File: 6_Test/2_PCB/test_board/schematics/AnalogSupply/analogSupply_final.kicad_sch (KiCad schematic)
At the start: 17 parts

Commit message: Corrections to schematic 11_20_24
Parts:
- C? (x4): value CL05B104KP5NNNC -> 100n
- C? (x3): value CL10A475KP8NNNC -> 4.7u
- R?: value RC0402JR-071KL -> 1k
- R?: value RC0402JR-071KL -> 4.7k
- R? (x3): value PV37W103C01B00 -> 10k
- U? (x2): footprint KS-6_ADI -> opampADA4807Footprints:KS-6_ADI
- U?: value TPS74501PDRVR -> LDO_Analog_Supply
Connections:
- net AVSS: no longer C?.1, C?.2
- net GND: now also C?.1, C?.2
- net at R?.2, U?.2 (FB): no longer R?.2
- net at R?.3: now also R?.2
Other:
- moved on the sheet: C?, L?, R?

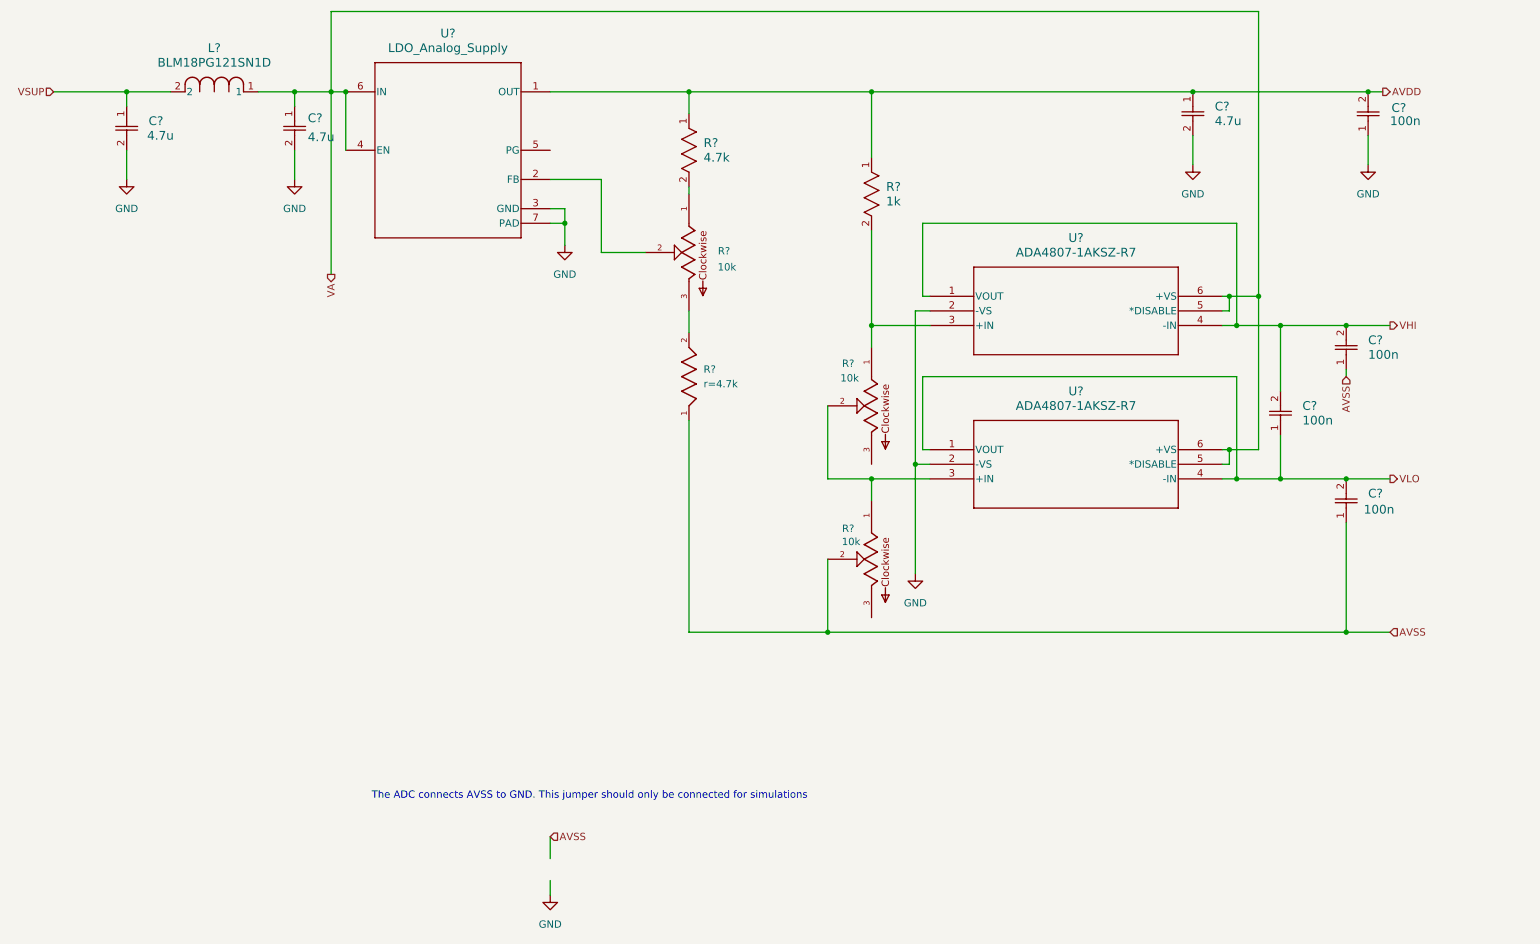
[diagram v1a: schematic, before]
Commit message: Revert "Corrections to schematic 11_20_24"
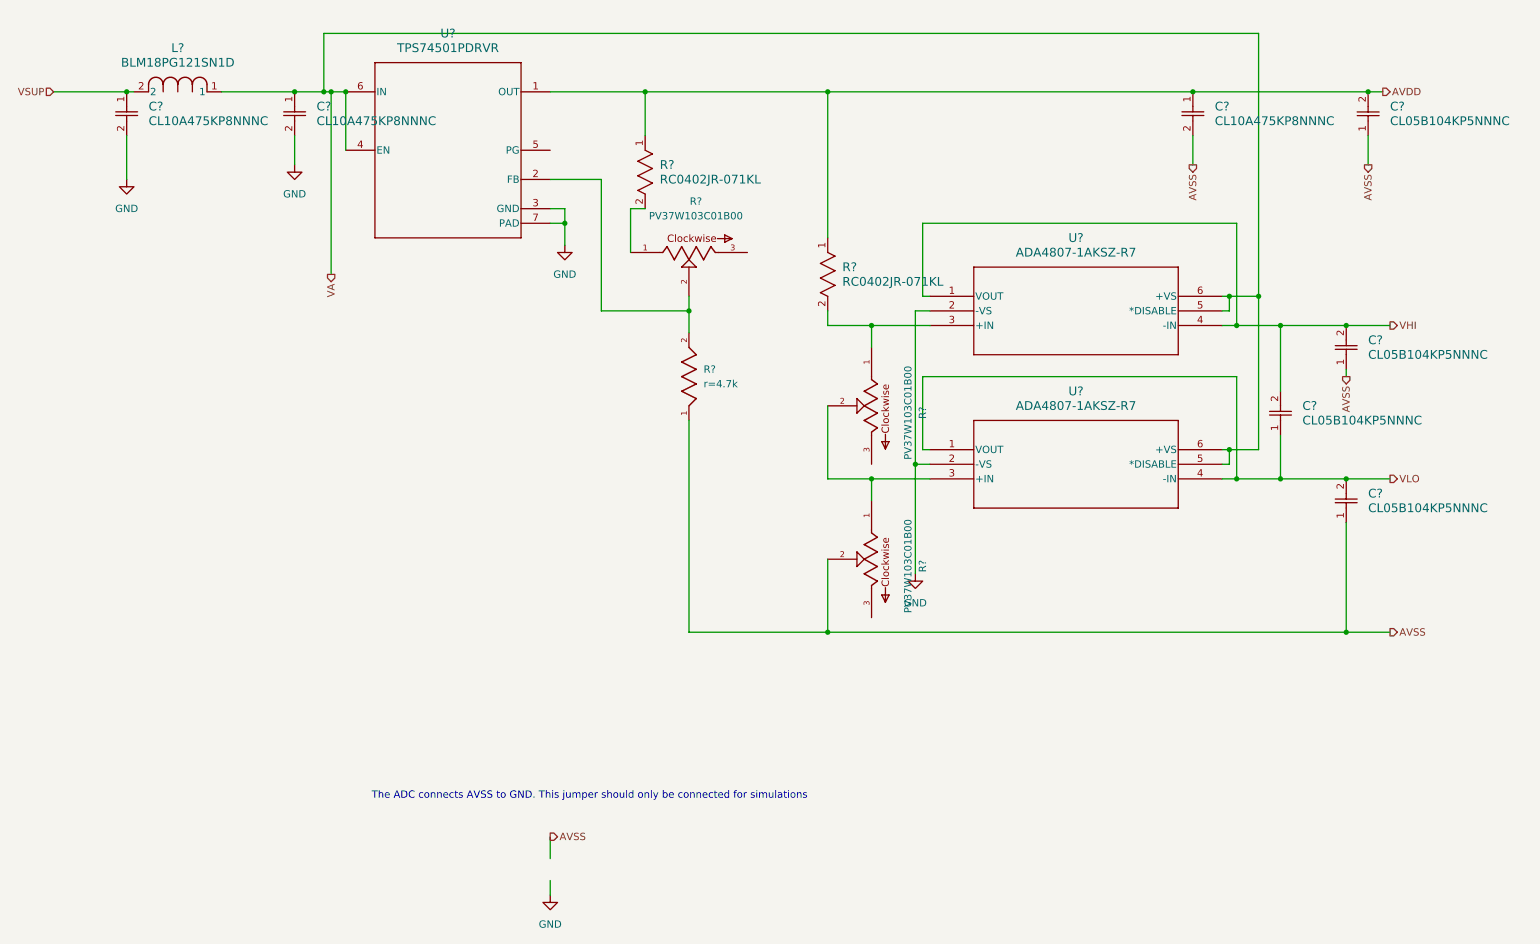
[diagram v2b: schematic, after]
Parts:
- C? (x4): value 100n -> CL05B104KP5NNNC
- C? (x3): value 4.7u -> CL10A475KP8NNNC
- R?: value 1k -> RC0402JR-071KL
- R?: value 4.7k -> RC0402JR-071KL
- R? (x3): value 10k -> PV37W103C01B00
- U? (x2): footprint opampADA4807Footprints:KS-6_ADI -> KS-6_ADI
- U?: value LDO_Analog_Supply -> TPS74501PDRVR
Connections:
- net AVSS: now also C?.1, C?.2
- net GND: no longer C?.1, C?.2
- net at R?.2: now also R?.2, U?.2 (FB); no longer R?.3
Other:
- moved on the sheet: C?, L?, R?
